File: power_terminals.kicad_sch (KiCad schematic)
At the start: 57 parts, among them J1 Screw_Terminal_01x02, Q1 SiS443DN, T1 GND, T10 V_{BUS}, T12 5V, T14 V_{BUS}_SENSE, T32 GND, T6 V_{DC}_SENSE, T9 V_{DC}, U5 TPS54240DRC

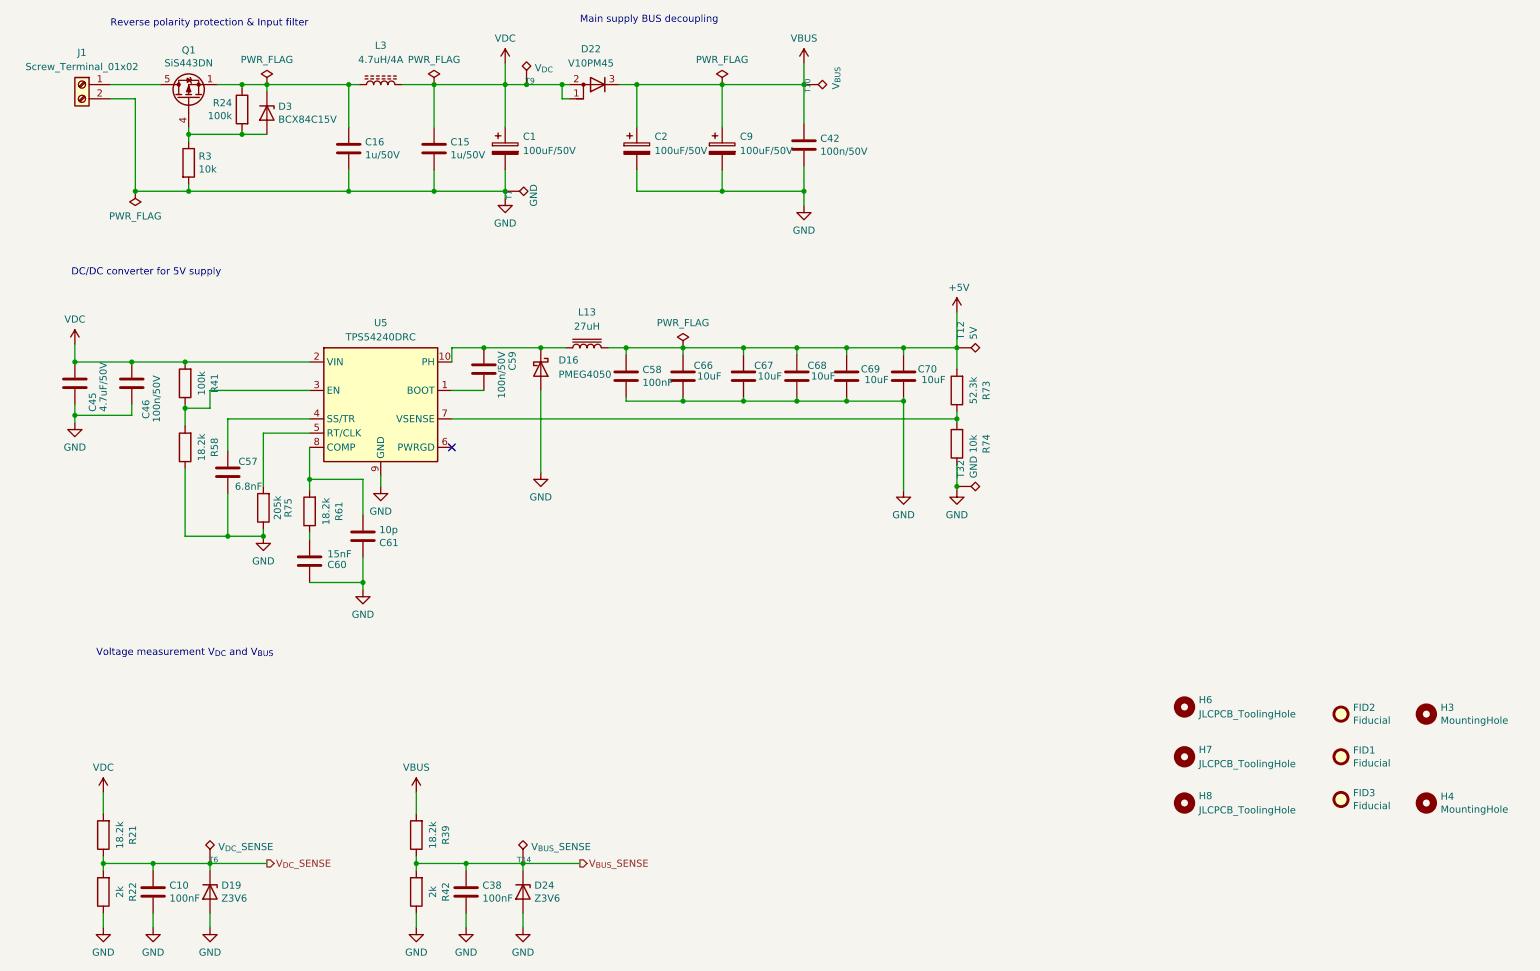
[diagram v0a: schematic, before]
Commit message: Simplified design (Old version switched to hodor-max)
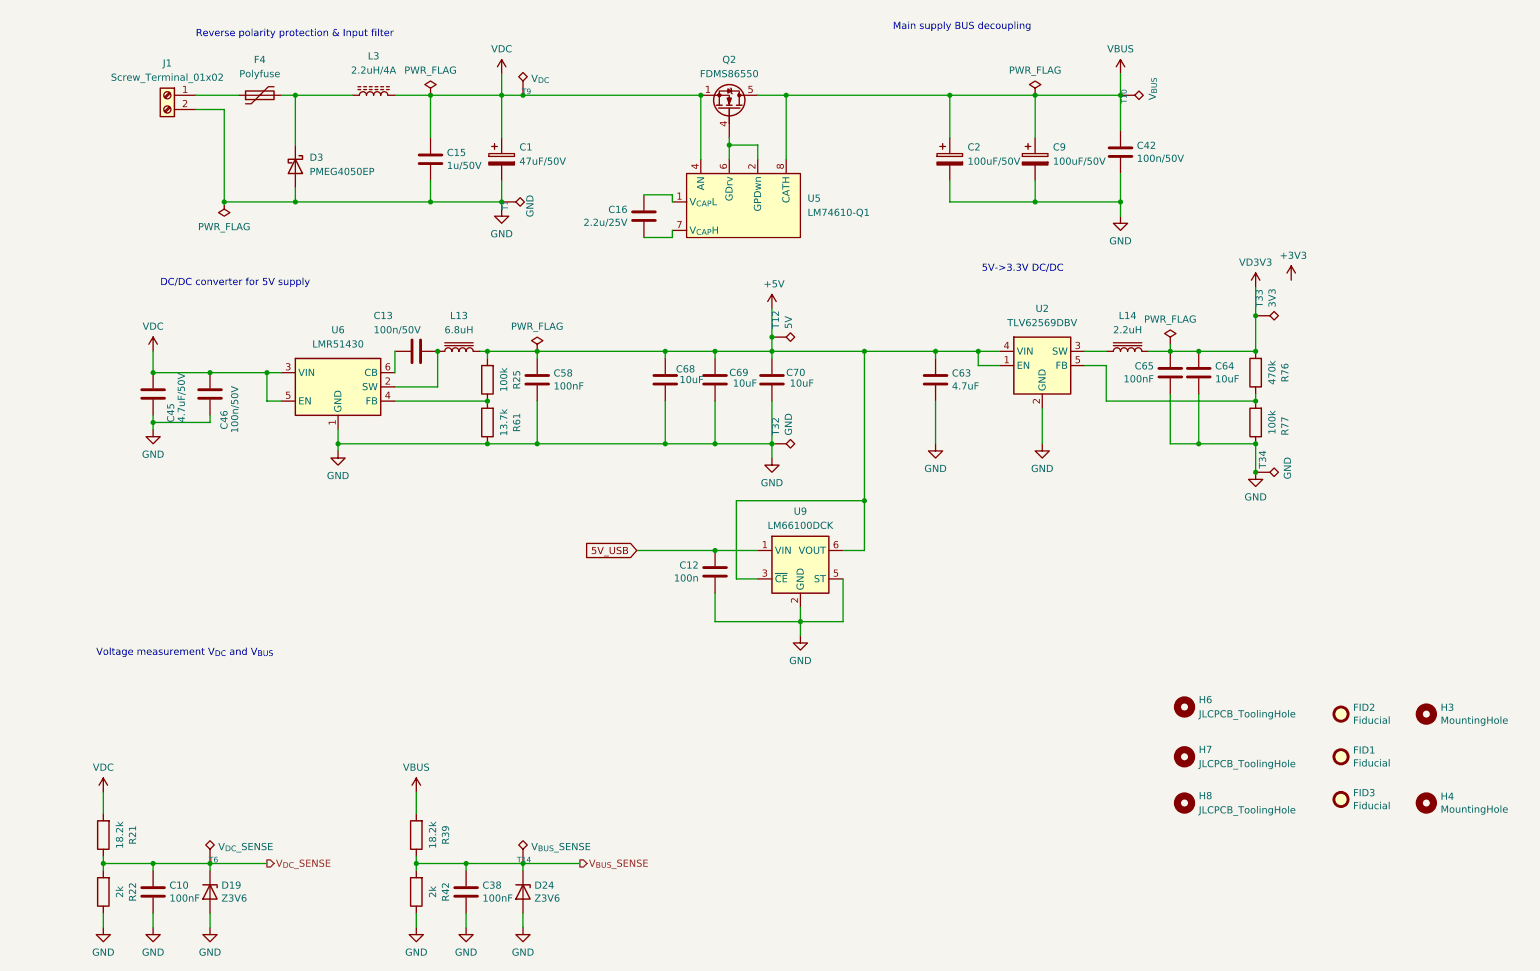
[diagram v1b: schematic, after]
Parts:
- removed C57: 6.8nF, Capacitor_SMD:C_0402_1005Metric, symbol Device:C
- removed C59: 100n/50V, Capacitor_SMD:C_0603_1608Metric, symbol Device:C
- removed C60: 15nF, Capacitor_SMD:C_0402_1005Metric, symbol Device:C
- removed C61: 10p, Capacitor_SMD:C_0402_1005Metric, symbol Device:C
- removed C66, C67: 10uF, Capacitor_SMD:C_0805_2012Metric, symbol Device:C
- removed D16: PMEG4050, Diode_SMD:D_SMB, symbol Device:D_Schottky
- removed D22: V10PM45, Package_TO_SOT_SMD:TO-277A, symbol Device:D_AAK
- removed D3: BCX84C15V, Diode_SMD:D_SOD-523, symbol Device:D_Zener
- removed Q1: SiS443DN, Package_SO:Vishay_PowerPAK_1212-8_Single, symbol Transistor_FET:SiS443DN
- removed R24, R41: 100k, Resistor_SMD:R_0402_1005Metric, symbol Device:R
- removed R3, R74: 10k, Resistor_SMD:R_0402_1005Metric, symbol Device:R
- removed R58: 18.2k, Resistor_SMD:R_0402_1005Metric, symbol Device:R
- removed R73: 52.3k, Resistor_SMD:R_0402_1005Metric, symbol Device:R
- removed R75: 205k, Resistor_SMD:R_0402_1005Metric, symbol Device:R
- removed U5: TPS54240DRC, Package_SON:Texas_DRC0010J_ThermalVias, symbol Converter_DCDC:TPS54240DRC
- added C12: 100n, Capacitor_SMD:C_0402_1005Metric, symbol Device:C
- added C13: 100n/50V, Capacitor_SMD:C_0603_1608Metric, symbol Device:C
- added C63: 4.7uF, Capacitor_SMD:C_1206_3216Metric, symbol Device:C
- added C64: 10uF, Capacitor_SMD:C_0805_2012Metric, symbol Device:C
- added C65: 100nF, Capacitor_SMD:C_0402_1005Metric, symbol Device:C
- added D3: PMEG4050EP, Diode_SMD:D_SOD-128, symbol Diode:PMEG4050EP
- added F4: Polyfuse, Fuse:Fuse_2920_7451Metric, symbol Device:Polyfuse
- added L14: 2.2uH, Inductor_SMD:L_1812_4532Metric, symbol Device:L_Iron
- added Q2: FDMS86550, Package_TO_SOT_SMD:TDSON-8-1, symbol Transistor_FET:FDMS86550
- added R25, R77: 100k, Resistor_SMD:R_0402_1005Metric, symbol Device:R
- added R76: 470k, Resistor_SMD:R_0402_1005Metric, symbol Device:R
- added T33: 3V3, TestPoint:TestPoint_Pad_D1.0mm, symbol Connector:TestPoint_Alt
- added T34: GND, TestPoint:TestPoint_Pad_1.0x1.0mm, symbol Connector:TestPoint_Alt
- added U2: TLV62569DBV, Package_TO_SOT_SMD:SOT-23-5, symbol Regulator_Switching:TLV62569DBV
- added U5: LM74610-Q1, Package_SO:VSSOP-8_3x3mm_P0.65mm, symbol hodor_custom_parts:LM74610
- added U6: LMR51430, Package_TO_SOT_SMD:SOT-23-6, symbol Regulator_Switching:LMR51430
- added U9: LM66100DCK, Package_TO_SOT_SMD:SOT-363_SC-70-6, symbol Power_Management:LM66100DCK
- C1: value 100uF/50V -> 47uF/50V; footprint Capacitor_SMD:C_Elec_8x10.2 -> Capacitor_SMD:CP_Elec_6.3x5.8
- C16: value 1u/50V -> 2.2u/25V
- L13: value 27uH -> 6.8uH; footprint Inductor_SMD:L_Wuerth_WE-PD-Typ-7345 -> Inductor_SMD:L_Wuerth_WE-PD2-Typ-MS
- L3: value 4.7uH/4A -> 2.2uH/4A
- R61: value 18.2k -> 13.7k
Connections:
- net +5V: now also C63.1, R25.2, U2.1 (EN), U2.4 (VIN), U9.3 (~{CE}), U9.6 (VOUT)
- net GND: now also R61.1, C12.1, C63.2, C64.2, C65.2, D3.2 (A), R77.1, T34.1, U2.2 (GND), U6.1 (GND), U9.2 (GND), U9.5 (ST); no longer C16.2
- net VBUS: now also Q2.5 (D), U5.8 (CATH)
- net VDC: now also Q2.1 (S), Q2.2 (S), Q2.3 (S), U5.4 (AN), U6.3 (VIN), U6.5 (EN)
- net at L3.1: now also D3.1 (K), F4.2; no longer C16.1
- net at J1.1 (Pin_1): now also F4.1
- net at R61.2: now also R25.1, U6.4 (FB)
- net at L13.1: now also C13.1, U6.2 (SW)
- new net: C16.1, U5.1 (V_{CAP}L)
- new net: Q2.4 (G), U5.2 (GPDwn), U5.6 (GDrv)
- new net: C16.2, U5.7 (V_{CAP}H)
- new net: L14.1, U2.3 (SW)
- new net: R76.1, R77.2, U2.5 (FB)
- new net: C13.2, U6.6 (CB)
- new net 5V_USB: C12.2, U9.1 (VIN)
- new net VD3V3: C64.1, C65.1, L14.2, R76.2, T33.1
- no-connect marks 1 -> 0
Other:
- note added: "5V->3.3V DC/DC"
- moved on the sheet: C1, C15, C2, C42, C45, C46, C58, C68, C69, C70, C9, J1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

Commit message: All nets connected
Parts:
- removed T34: GND, TestPoint:TestPoint_Pad_1.0x1.0mm, symbol Connector:TestPoint_Alt
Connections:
- net VD3V3 is gone; now on net +3V3: C64.1, C65.1, L14.2, R76.2, T33.1
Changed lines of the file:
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@@
 	)
 	(junction
-		(at 233.68 100.33)
-		(diameter 0)
-		(color 0 0 0 0)
-	)
-	(junction
 		(at 218.44 78.74)
 		(diameter 0)
@@
 	)
 	(symbol
-		(lib_id "Connector:TestPoint_Alt")
-		(at 233.68 100.33 270)
-		(unit 1)
-		(exclude_from_sim no)
-		(in_bom no)
-		(on_board yes)
-		(dnp no)
-		(property "Reference" "T34"
-			(at 234.95 99.695 0)
-			(effects
-				(font
-					(size 1.27 1.27)
-				)
-				(justify right)
-			)
-		)
-		(property "Value" "GND"
-			(at 239.395 101.6 0)
-			(effects
-				(font
-					(size 1.27 1.27)
-				)
-				(justify right)
-			)
-		)
-		(property "Footprint" "TestPoint:TestPoint_Pad_1.0x1.0mm"
-			(at 233.68 105.41 0)
-			(effects
-				(font
-					(size 1.27 1.27)
-				)
-				(hide yes)
-			)
-		)
-		(property "Datasheet" "~"
-			(at 233.68 105.41 0)
-			(effects
-				(font
-					(size 1.27 1.27)
-				)
-				(hide yes)
-			)
-		)
-		(property "Description" "test point (alternative shape)"
-			(at 233.68 100.33 0)
-			(effects
-				(font
-					(size 1.27 1.27)
-				)
-				(hide yes)
-			)
-		)
-		(pin "1"
-		)
-		(instances
-			(project "hodor_hardware"
-				(path "/2da01e60-41ef-423d-82f4-a5c8908d8b96/4a2ab631-9c09-4ff5-b76c-afe5090e4ede"
-					(reference "T34")
-					(unit 1)
-				)
-			)
-		)
-	)
-	(symbol
 		(lib_id "Device:C")
 		(at 36.83 86.36 0)
@@
 	)
 	(symbol
-		(lib_id "power:VD")
-		(at 233.68 67.31 0)
-		(unit 1)
-		(exclude_from_sim no)
-		(in_bom yes)
-		(on_board yes)
-		(dnp no)
-		(fields_autoplaced yes)
-		(property "Reference" "#PWR05"
-			(at 233.68 71.12 0)
-			(effects
-				(font
-					(size 1.27 1.27)
-				)
-				(hide yes)
-			)
-		)
-		(property "Value" "VD3V3"
-			(at 233.68 62.865 0)
-			(effects
-				(font
-					(size 1.27 1.27)
-				)
-			)
-		)
-		(property "Footprint" ""
-			(at 233.68 67.31 0)
-			(effects
-				(font
-					(size 1.27 1.27)
-				)
-				(hide yes)
-			)
-		)
-		(property "Datasheet" ""
-			(at 233.68 67.31 0)
-			(effects
-				(font
-					(size 1.27 1.27)
-				)
-				(hide yes)
-			)
-		)
-		(property "Description" "Power symbol creates a global label with name \"VD\""
-			(at 233.68 67.31 0)
-			(effects
-				(font
-					(size 1.27 1.27)
-				)
-				(hide yes)
-			)
-		)
-		(pin "1"
-		)
-		(instances
-			(project "hodor_hardware"
-				(path "/2da01e60-41ef-423d-82f4-a5c8908d8b96/4a2ab631-9c09-4ff5-b76c-afe5090e4ede"
-					(reference "#PWR05")
-					(unit 1)
-				)
-			)
-		)
-	)
-	(symbol
 		(lib_id "hodor_custom_parts:LM74610")
 		(at 142.24 52.07 0)
@@
 	(symbol
 		(lib_id "power:+3V3")
-		(at 240.03 66.04 0)
+		(at 233.68 67.31 0)
 		(unit 1)
 		(exclude_from_sim no)
@@
 		(dnp no)
 		(property "Reference" "#PWR035"
-			(at 240.03 69.85 0)
+			(at 233.68 71.12 0)
 			(effects
 				(font
@@
 		)
 		(property "Value" "+3V3"
-			(at 240.411 61.6458 0)
+			(at 234.061 62.9158 0)
 			(effects
 				(font
@@
 		)
 		(property "Footprint" ""
-			(at 240.03 66.04 0)
+			(at 233.68 67.31 0)
 			(effects
 				(font
@@
 		)
 		(property "Datasheet" ""
-			(at 240.03 66.04 0)
+			(at 233.68 67.31 0)
 			(effects
 				(font
@@
 		)
 		(property "Description" "Power symbol creates a global label with name \"+3V3\""
-			(at 240.03 66.04 0)
+			(at 233.68 67.31 0)
 			(effects
 				(font

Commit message: Finalized Layout
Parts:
- C22: renamed from C12; value 100n -> 100nF
- R14: renamed from R42; value 2k -> 2.2k
- R8: renamed from R22; value 2k -> 2.2k
- renumbered C16 to C10, C45 to C11, C46 to C12, C68 to C14, C69 to C15, C58 to C16, C70 to C17, C9 to C18, C38 to C20, C63 to C21, C65 to C25, C64 to C26, C2 to C27, C42 to C38, C15 to C4, C1 to C8, C10 to C9, D24 to D11, D3 to D4, D19 to D8, F4 to F1, FID3 to FID2, FID2 to FID3, H7 to H1, H3 to H2, H4 to H3, H8 to H4, H6 to H5, L3 to L4, L13 to L5, L14 to L7, R61 to R11, R25 to R12, R39 to R13, R77 to R16, R76 to R17, R21 to R7, T6 to T1, T32 to T11, T1 to T2, T9 to T6, T12 to T7, T14 to T8, T33 to T9, U5 to U4, U6 to U5, U9 to U6, U2 to U7
